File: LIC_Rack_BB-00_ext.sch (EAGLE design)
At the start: 6 parts, among them Q1 IRLL014

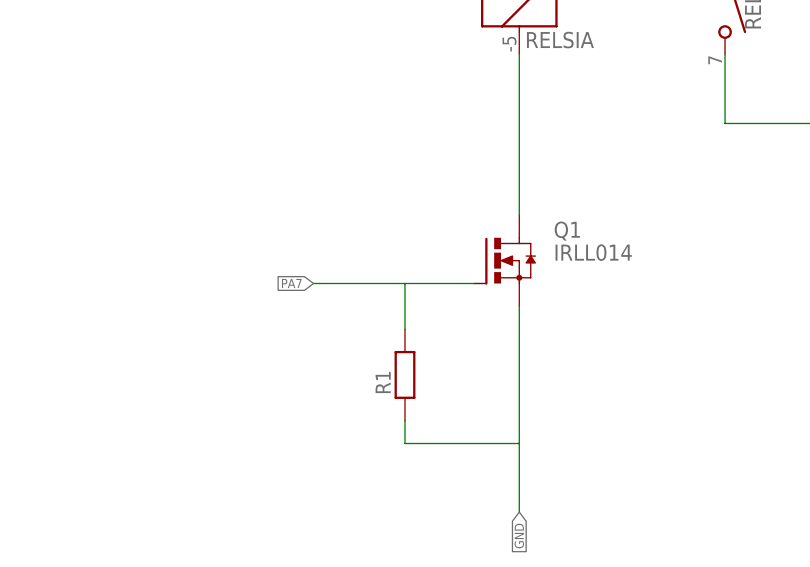
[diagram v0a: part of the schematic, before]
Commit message: Pridána nová verze
Přidána nová verze zkráceno na 4 In a 4 Out a přidáno relé na desku
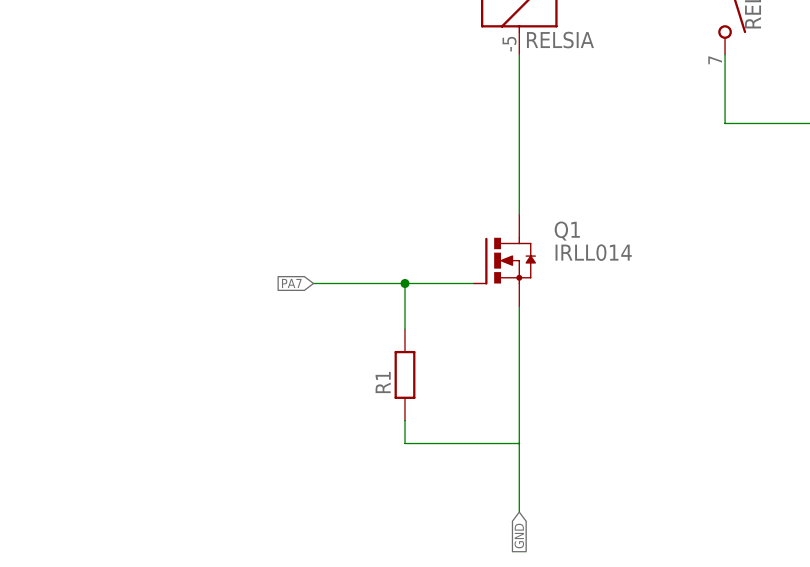
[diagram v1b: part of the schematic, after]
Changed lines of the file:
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@@
 <drawing>
 <settings>
-<setting alwaysvectorfont="no"/>
+<setting alwaysvectorfont="yes"/>
 <setting verticaltext="up"/>
 </settings>
@@
 <wire x1="68.58" y1="101.6" x2="58.42" y2="101.6" width="0.1524" layer="91"/>
 <label x="58.42" y="101.6" size="1.016" layer="95" rot="R180" xref="yes"/>
+<junction x="68.58" y="101.6"/>
 </segment>
 <segment>
